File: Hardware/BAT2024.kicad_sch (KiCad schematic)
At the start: 0 parts

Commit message: Finalized schematic V1.0; minor changes to symbol library
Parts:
- added C1, C2, C5, C6, C7, C8: 1uF, symbol Device:C
- added C10, C9: 100nF, symbol Device:C
- added C3, C4: 0.47uF, symbol Device:C
- added D1: LED, symbol Device:LED
- added F1: Littlefuse_1210L020WR, BAT_Footprint-Library:Littlefuse_FUSC3226X100N, symbol BAT_Library:Littlefuse_1210L020WR
- added H1: BatteryHolder_1025-7, BAT_Footprint-Library:BatteryHolder_10257, symbol BAT_Library:BatteryHolder_1025-7
- added H2, H3, H4, H5: MountingHole, MountingHole:MountingHole_3.2mm_M3, symbol Mechanical:MountingHole
- added IC1: BGM220PC22WGA2R, BAT_Footprint-Library:BGM220PC22WGA2R, symbol BAT_Library:BGM220PC22WGA2R
- added IC2: EEPROM_M95P16-IXMNT_E, BAT_Footprint-Library:EEPROM_SOIC127P600X175-8L, symbol BAT_Library:EEPROM_M95P16-IXMNT_E
- added IC3: LED-Driver_LP55231SQX_NOPB, BAT_Footprint-Library:LED-Driver-QFN50P400X400X80-25N, symbol BAT_Library:LED-Driver_LP55231SQX_NOPB
- added J1: Conn_ARM_SWD_TagConnect_TC2030-NL, Connector:Tag-Connect_TC2030-IDC-NL_2x03_P1.27mm_Vertical, symbol Connector:Conn_ARM_SWD_TagConnect_TC2030-NL
- added J2: USB4105-GF-A-060, BAT_Footprint-Library:GCT_USB4105-GF-A-060, symbol BAT_Library:USB4105-GF-A-060
- added LED1, LED2, LED3, LED4, LED5, LED6, LED7, LED8: LED_XZCM2CRK53WA-8VF, BAT_Footprint-Library:LEDM168X110N, symbol BAT_Library:LED_XZCM2CRK53WA-8VF
- added MK1: MEMS-Microphone_ICS-41351, BAT_Footprint-Library:MEMS-Mikrofon_ICS41351, symbol BAT_Library:MEMS-Microphone_ICS-41351
- added R1, R2: 5.1k, symbol Device:R
- added R3, R4, R5, R6, R7, R8: 10k, symbol Device:R
- added S1: JS102011SAQN, BAT_Footprint-Library:C-K_Switch_JS102011SAQN, symbol BAT_Library:JS102011SAQN
- added TP1: VCC, BAT_Footprint-Library:TestPoint_Pad_1.5x1.5mm, symbol BAT_Library:TestPoint
- added TP10: MOSI, BAT_Footprint-Library:TestPoint_Pad_1.5x1.5mm, symbol BAT_Library:TestPoint
- added TP11: MISO, BAT_Footprint-Library:TestPoint_Pad_1.5x1.5mm, symbol BAT_Library:TestPoint
- added TP12: CLK, BAT_Footprint-Library:TestPoint_Pad_1.5x1.5mm, symbol BAT_Library:TestPoint
- added TP13: PDM_CLK, BAT_Footprint-Library:TestPoint_Pad_1.5x1.5mm, symbol BAT_Library:TestPoint
- added TP14: PDM_DATA0, BAT_Footprint-Library:TestPoint_Pad_1.5x1.5mm, symbol BAT_Library:TestPoint
- added TP2: +BATT, BAT_Footprint-Library:TestPoint_Pad_1.5x1.5mm, symbol BAT_Library:TestPoint
- added TP3: +3V3, BAT_Footprint-Library:TestPoint_Pad_1.5x1.5mm, symbol BAT_Library:TestPoint
- added TP4, TP5, TP6: GND, BAT_Footprint-Library:TestPoint_Pad_1.5x1.5mm, symbol BAT_Library:TestPoint
- added TP7: SDA, BAT_Footprint-Library:TestPoint_Pad_1.5x1.5mm, symbol BAT_Library:TestPoint
- added TP8: SCL, BAT_Footprint-Library:TestPoint_Pad_1.5x1.5mm, symbol BAT_Library:TestPoint
- added TP9: CS, BAT_Footprint-Library:TestPoint_Pad_1.5x1.5mm, symbol BAT_Library:TestPoint
- added U1: MIC5504-3.3YM5, Package_TO_SOT_SMD:SOT-23-5, symbol BAT_Library:MIC5504-3.3YM5
- added U2: BQ21040DBVR, BAT_Footprint-Library:BatteryManagement_SOT95P280X145-6N, symbol BAT_Library:BQ21040DBVR
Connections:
- new net: J2.A5 (CC1), R1.2
- new net: D1.1 (K), U2.3 (~{CHG})
- new net: D1.2 (A), R3.1
- new net: R4.1, U2.1 (TS)
- new net: S1.1, U1.5 (VOUT)
- new net: F1.2, U2.6 (VIN)
- new net: R5.1, U2.4 (ISET)
- new net: J2.B5 (CC2), R2.2
- new net +3.3V: C1.1, C10.1, C6.1, C8.1, C9.1, IC1.13 (VDD), IC2.3 (~{W-DQ2}), IC2.7 (~{HOLD-DQ3}), IC2.8 (VCC), IC3.3 (VDD), MK1.1 (VDD), R6.1, R7.1, R8.1, S1.2, TP3.1
- new net +BATT: C7.1, H1.2 (+), R3.2, TP2.1, U1.1 (VIN), U1.3 (EN), U2.2 (OUT)
- new net C1+: C3.1, IC3.2 (C1+)
- new net C1-: C3.2, IC3.24 (C1-)
- new net C2+: C4.1, IC3.1 (C2+)
- new net C2-: C4.2, IC3.23 (C2-)
- new net DRV_EN: IC1.11 (PA04), IC3.5 (EN)
- new net DRV_VOUT: C2.1, IC3.22 (VOUT)
- new net GND: C1.2, C10.2, C2.2, C5.2, C6.2, C7.2, C8.2, C9.2, H1.1 (-), IC1.1 (GND_1), IC1.12 (GND_2), IC1.20 (GND_3), IC1.31 (GND_4), IC2.4 (VSS), IC3.20 (ASEL0), IC3.21 (ASEL1), IC3.25 (GND_2), IC3.4 (GND_1), IC3.6 (CLK), J1.5 (GND), J2.A1_B12 (GND), J2.B1_A12 (GND), J2.SH1 (SHELL_GND), J2.SH2 (SHELL_GND), J2.SH3 (SHELL_GND), J2.SH4 (SHELL_GND), LED1.1, LED2.1, LED3.1, LED4.1, LED5.1, LED6.1, LED7.1, LED8.1, MK1.4 (GND_1), MK1.5 (SELECT), MK1.6 (GND_2), R1.1, R2.1, R4.2, R5.2, TP4.1, TP5.1, TP6.1, U1.2 (GND), U2.5 (GND)
- new net I2C_SCL: IC1.29 (PC07), IC3.9 (SCL), R8.2, TP8.1
- new net I2C_SDA: IC1.28 (PC06), IC3.8 (SDA), R7.2, TP7.1
- new net I2S_SCK: IC1.2 (PB04)
- new net I2S_SD: IC1.3 (PB03)
- new net I2S_WS: IC1.4 (PB02)
- new net LED1: IC3.19 (D1), LED1.2
- new net LED2: IC3.18 (D2), LED2.2
- new net LED3: IC3.17 (D3), LED3.2
- new net LED4: IC3.16 (D4), LED4.2
- new net LED5: IC3.15 (D5), LED5.2
- new net LED6: IC3.14 (D6), LED6.2
- new net LED7: IC3.13 (D7), LED7.2
- new net LED8: IC3.12 (D8), LED8.2
- new net PDM_CLK: IC1.7 (PA00), MK1.2 (CLK), TP13.1
- new net PDM_DATA0: IC1.6 (PB00), MK1.3 (DATA), TP14.1
- new net PDM_DATA1: IC1.5 (PB01)
- new net PTI_DATA: IC1.26 (PC04)
- new net PTI_FRAME: IC1.27 (PC05)
- new net RESET: IC1.30 (RESETN), J1.3 (~{RESET}), J2.A7 (DN1)
- new net SPI_CS: IC1.24 (PC02), IC2.1 (~{S}_/_CS), R6.2, TP9.1
- new net SPI_MISO: IC1.22 (PC00), IC2.2 (Q-DQ1), TP11.1
- new net SPI_MOSI: IC1.23 (PC01), IC2.5 (D-DQ0), TP10.1
- new net SPI_SCK: IC1.25 (PC03), IC2.6 (C), TP12.1
- new net SWCLK: IC1.8 (PA01), J1.4 (SWCLK), J2.B6 (DP2)
- new net SWDIO: IC1.9 (PA02), J1.2 (SWDIO), J2.B7 (DN2)
- new net SWO: IC1.10 (PA03), J1.6 (SWO), J2.A6 (DP1)
- new net VCC: C5.1, F1.1, J1.1 (VCC), J2.A4_B9 (VBUS), J2.B4_A9 (VBUS), TP1.1
- no-connect marks 0 -> 18
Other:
- note added: "Auxiliary components"
- note added: "BMS"
- note added: "CS: low active DQ2: low active DQ3: low active"
- note added: "Disable temp sense"
- note added: "EEPROM"
- note added: "EN could also be left floating"
- note added: "I2C"
- note added: "I2C-Addr: 0x32"
- note added: "LDO"
- note added: "LED"
- note added: "LED Driver"
- note added: "M3-Screwholes"
- note added: "MIC"
- note added: "Mechanical"
- note added: "Microcontroller"
- note added: "Microphone"
- note added: "Power"
- note added: "Programmed charge-current: Fast-Charge = 50mA"
- note added: "R_ISET: 60mA < I < 1000mA => 540 / I 25mA < I < 60mA => 527 / I 10mA < I < 25mA => 520 / I"
- note added: "Select tied to GND => DATA 1 / right channel"
- note added: "Testpoints"
- note added: "USB-C & Debug & Programming"
- note added: "does not need external pullup resistor low active"

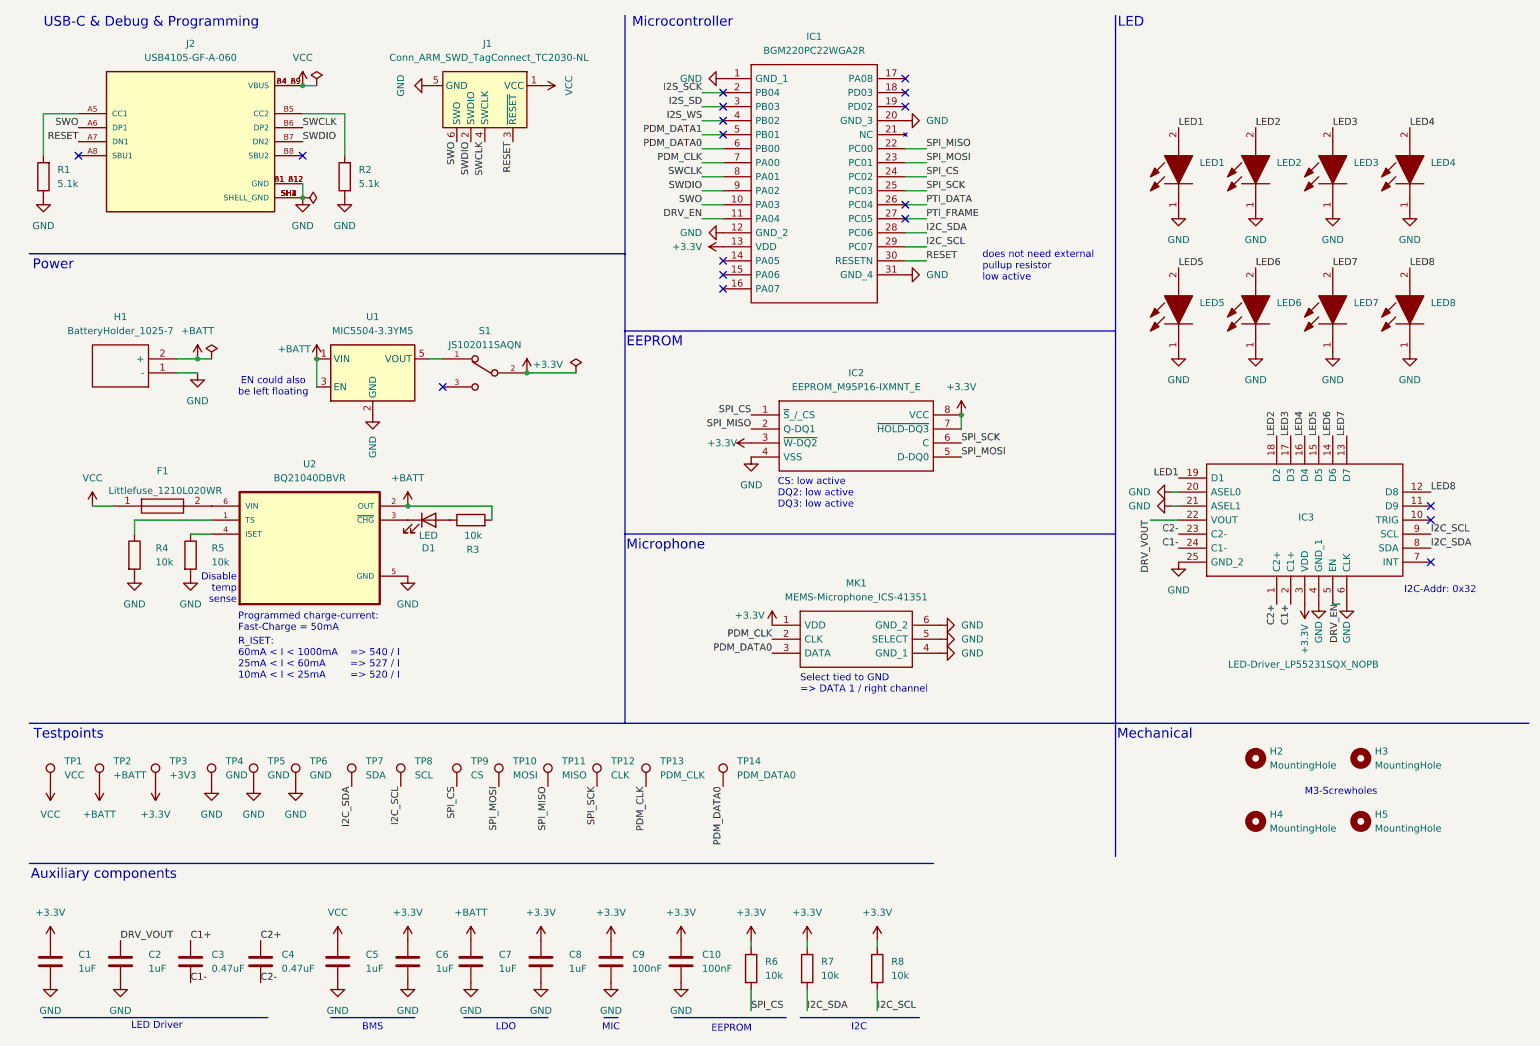
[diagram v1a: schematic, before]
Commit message: Add temporary layout of footprints on PCB; generate placement-pdf
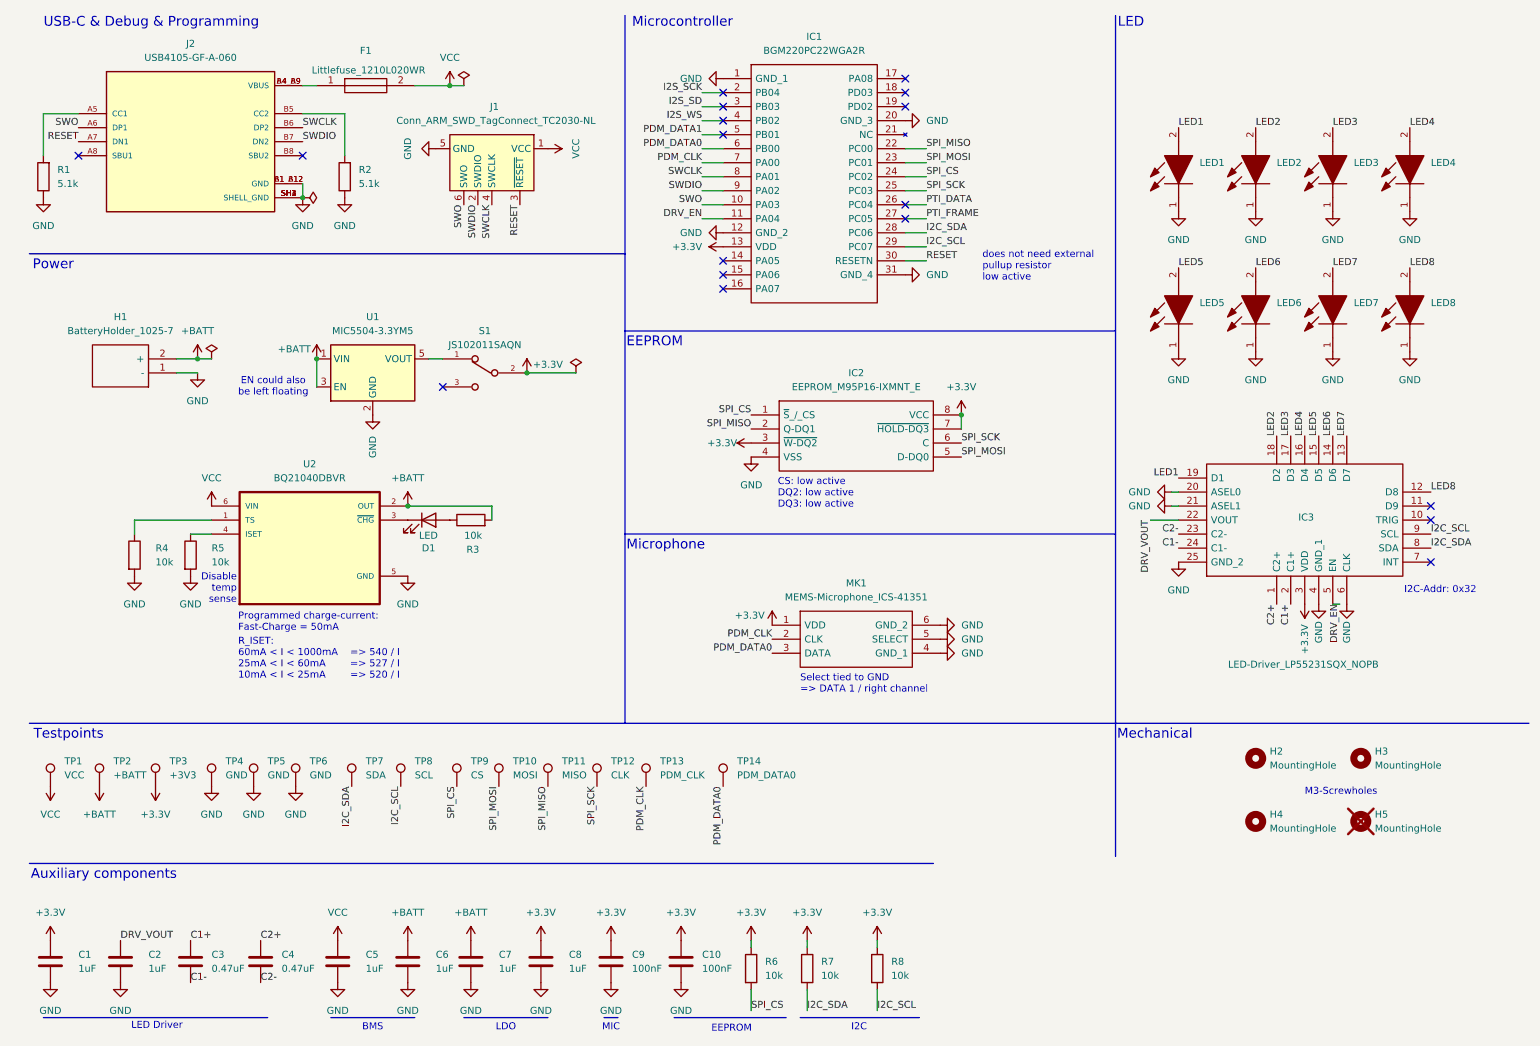
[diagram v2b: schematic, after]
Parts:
- C1, C10, C2, C3, C4, C5, C6, C7, C8, C9: footprint (none) -> Capacitor_SMD:C_0603_1608Metric_Pad1.08x0.95mm_HandSolder
- D1: footprint (none) -> LED_SMD:LED_0603_1608Metric_Pad1.05x0.95mm_HandSolder
- H5: now not fitted
- R1, R2, R3, R4, R5, R6, R7, R8: footprint (none) -> Resistor_SMD:R_0603_1608Metric_Pad0.98x0.95mm_HandSolder
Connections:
- net +3.3V: no longer C6.1
- net +BATT: now also C6.1
- net VCC: now also F1.2, U2.6 (VIN); no longer F1.1, J2.A4_B9 (VBUS), J2.B4_A9 (VBUS)
- new net: F1.1, J2.A4_B9 (VBUS), J2.B4_A9 (VBUS)
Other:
- moved on the sheet: F1, J1

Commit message: Created first layout
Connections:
- net +3.3V: now also J1.1 (VCC); no longer C8.1, TP3.1
- net RESET: now also J2.B7 (DN2); no longer J2.A7 (DN1)
- net SWDIO: now also J2.A7 (DN1); no longer J2.B7 (DN2)
- net VCC: no longer J1.1 (VCC)
- net +3.3: now reaches S1.1, U1.5 (VOUT)
- net +3.3: now also C8.1, TP3.1
- net Fuse: now reaches F1.1, J2.A4_B9 (VBUS), J2.B4_A9 (VBUS)
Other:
- moved on the sheet: F1, S1

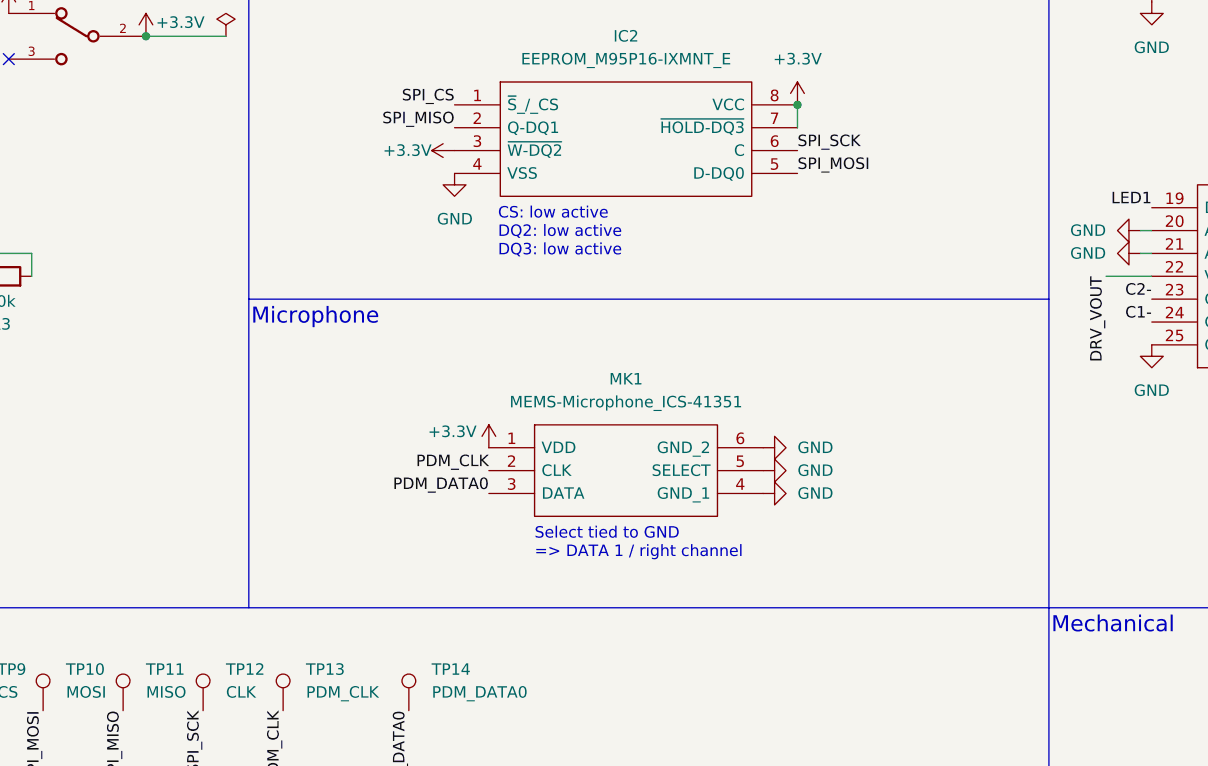
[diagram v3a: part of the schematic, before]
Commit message: Add IC outline to schematic; Add iBom for V1-1
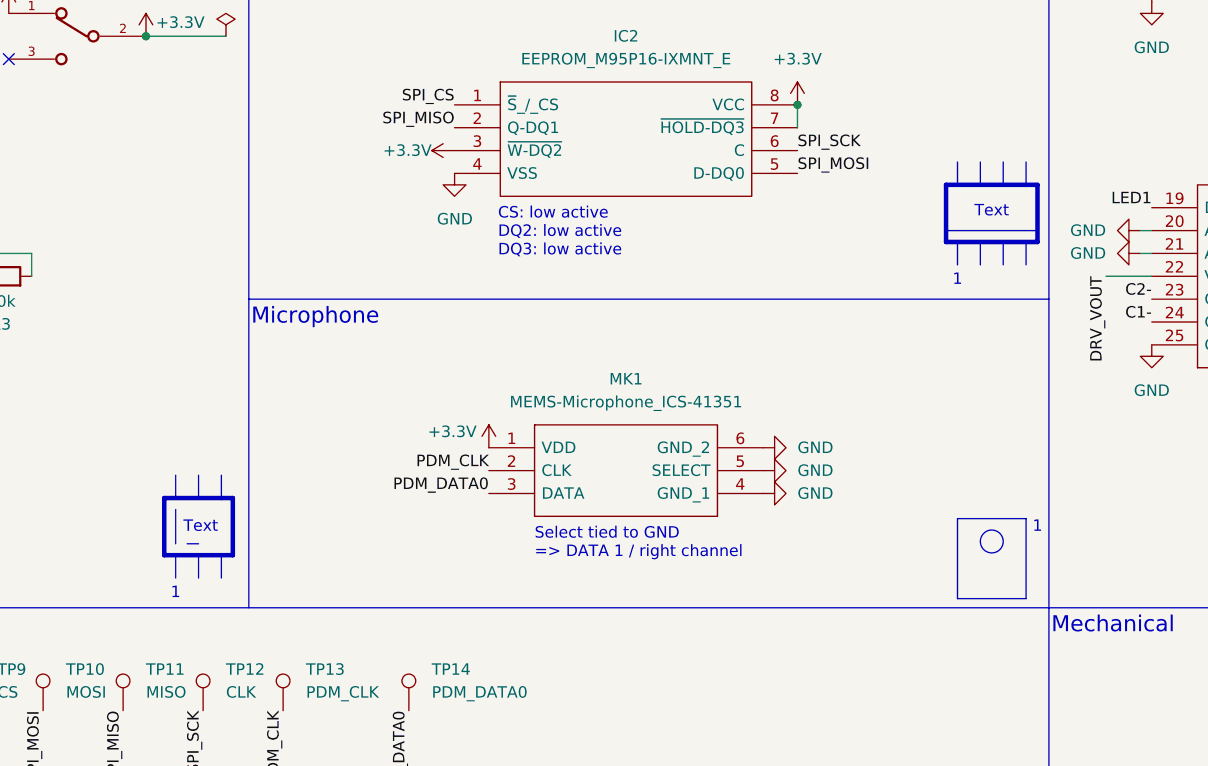
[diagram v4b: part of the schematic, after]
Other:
- note added: "1"
- note added: "Text"

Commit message: Created PCB V1-2; see documentation for changelog
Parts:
- removed J2: USB4105-GF-A-060, BAT_Footprint-Library:GCT_USB4105-GF-A-060, symbol BAT_Library:USB4105-GF-A-060
- removed TP10: MOSI, BAT_Footprint-Library:TestPoint_Pad_1.5x1.5mm, symbol BAT_Library:TestPoint
- removed TP11: MISO, BAT_Footprint-Library:TestPoint_Pad_1.5x1.5mm, symbol BAT_Library:TestPoint
- removed TP12: CLK, BAT_Footprint-Library:TestPoint_Pad_1.5x1.5mm, symbol BAT_Library:TestPoint
- removed TP13: PDM_CLK, BAT_Footprint-Library:TestPoint_Pad_1.5x1.5mm, symbol BAT_Library:TestPoint
- removed TP14: PDM_DATA0, BAT_Footprint-Library:TestPoint_Pad_1.5x1.5mm, symbol BAT_Library:TestPoint
- removed TP5, TP6: GND, BAT_Footprint-Library:TestPoint_Pad_1.5x1.5mm, symbol BAT_Library:TestPoint
- removed TP7: SDA, BAT_Footprint-Library:TestPoint_Pad_1.5x1.5mm, symbol BAT_Library:TestPoint
- removed TP8: SCL, BAT_Footprint-Library:TestPoint_Pad_1.5x1.5mm, symbol BAT_Library:TestPoint
- removed TP9: CS, BAT_Footprint-Library:TestPoint_Pad_1.5x1.5mm, symbol BAT_Library:TestPoint
- added J1: USB4125-GF-A, BAT_Footprint-Library:USB4125GFA, symbol BAT_Library:USB4125-GF-A
- added Q1: SSM3J334R,LF, BAT_Footprint-Library:SSM3J334RLF, symbol BAT_Library:SSM3J334R,LF
- added R1, R2, R8: 10k, Resistor_SMD:R_0603_1608Metric_Pad0.98x0.95mm_HandSolder, symbol Device:R
- TP1, TP2, TP3, TP4: footprint BAT_Footprint-Library:TestPoint_Pad_1.5x1.5mm -> BAT_Footprint-Library:TestPoint_Pad_D1.0mm
- renumbered J1 to J2, R7 to R10, R8 to R11, R1 to R3, R2 to R4, R3 to R5, R4 to R6, R5 to R7, R6 to R9
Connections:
- net +3.3V: now also R8.2
- net +BATT: now also Q1.3; no longer U1.1 (VIN), U1.3 (EN)
- net DRV_EN: now also R8.1
- net Fuse: now also J1.A9 (VBUS_1), J1.B9 (VBUS_2), R1.2
- net GND: now also IC3.10 (TRIG), J1.A12 (GND_1), J1.B12 (GND_2), J1.MH1, J1.MH2, J1.MH3, J1.MH4, Q1.1, R2.1
- net at R3.2: now also J1.A5 (CC1)
- net Charge: now reaches IC1.19 (PD02)
- net Charge: now also R1.1, R2.2
- net at R4.2: now also J1.B5 (CC2)
- new net: Q1.2, U1.1 (VIN), U1.3 (EN)
- no-connect marks 18 -> 14
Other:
- note added: "3V3 Voltage Regulation"
- note added: "Battery"
- note added: "Reverse Polartity Protection"
- moved on the sheet: D1, F1, J2, R3, R4, R5, R6, R7, S1, U1, U2
